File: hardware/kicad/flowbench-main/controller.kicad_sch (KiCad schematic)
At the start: 11 parts, among them J4 ESP32-S3-DevKitC-1 J1, J5 ESP32-S3-DevKitC-1 J3

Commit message: KiCad: fix off-grid pins on ADS1219 and AM26C31 symbols
A floating-point modulo misread the symbol half-height as off-grid and
shifted it by half a step, leaving top and bottom pins 0.635 mm off the
1.27 mm connection grid (16 ERC warnings). verify.py now checks every pin
and wire end against the grid.

Co-Authored-By: Claude Opus 5.5 <noreply@anthropic.com>
Claude-Session: https://claude.ai/code/session_01QEmmugJA9S77dSDSNcKrPa
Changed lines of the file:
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@@
 (text "The DevKit plugs into two 22-pin sockets. Its own 3V3 pins are left open: the board makes +3V3 separately." (at 20.32 20.32 0) (effects (font (size 1.524 1.524)) (justify left bottom)))
 (text "GPIO35-37 are used by the octal flash and PSRAM. GPIO47/48 are 1.8 V on the WROOM-2 and stay unused." (at 20.32 24.13 0) (effects (font (size 1.524 1.524)) (justify left bottom)))
-(symbol (lib_id "FlowBench:DevKitC-1_J1") (at 29.21 71.12 0) (unit 1)
-  (in_bom yes) (on_board yes) (dnp no)
-  (property "Reference" "J4" (at 20.32 38.735 0) (effects (font (size 1.27 1.27)) (justify left)))
-  (property "Value" "ESP32-S3-DevKitC-1 J1" (at 25.06 38.735 0) (effects (font (size 1.27 1.27)) (justify left)))
-  (property "Footprint" "Connector_PinSocket_2.54mm:PinSocket_1x22_P2.54mm_Vertical" (at 29.21 71.12 0) (effects (font (size 1.27 1.27)) (justify left) hide))
-  (property "Datasheet" "~" (at 29.21 71.12 0) (effects (font (size 1.27 1.27)) (justify left) hide))
+(symbol (lib_id "FlowBench:DevKitC-1_J1") (at 29.21 69.85 0) (unit 1)
+  (in_bom yes) (on_board yes) (dnp no)
+  (property "Reference" "J4" (at 20.32 38.1 0) (effects (font (size 1.27 1.27)) (justify left)))
+  (property "Value" "ESP32-S3-DevKitC-1 J1" (at 25.06 38.1 0) (effects (font (size 1.27 1.27)) (justify left)))
+  (property "Footprint" "Connector_PinSocket_2.54mm:PinSocket_1x22_P2.54mm_Vertical" (at 29.21 69.85 0) (effects (font (size 1.27 1.27)) (justify left) hide))
+  (property "Datasheet" "~" (at 29.21 69.85 0) (effects (font (size 1.27 1.27)) (justify left) hide))
   (pin "1")
   (pin "2")
@@
   (pin "21")
   (pin "22")
-  (instances (project "flowbench-main" (path "/132431a4-6ccd-4deb-a1e9-9797cfc2cdf2/a3e77ddf-1815-4e9d-bd7e-a2f9fc3f67e3" (reference "J4") (unit 1))))
+  (instances (project "flowbench-main" (path "/c152861c-b5ff-4f41-8930-02e957d22356/ba051b45-4e57-4bb8-a5b4-557957ea72a9" (reference "J4") (unit 1))))
 )
 (no_connect (at 40.64 43.18))
@@
 (wire (pts (xy 40.64 96.52) (xy 43.18 96.52)) (stroke (width 0) (type default)))
 (global_label "GND" (shape passive) (at 43.18 96.52 0) (fields_autoplaced) (effects (font (size 1.27 1.27)) (justify left)) (property "Intersheetrefs" "${INTERSHEET_REFS}" (at 43.18 96.52 0) (effects (font (size 1.27 1.27)) (justify left) hide)))
-(symbol (lib_id "FlowBench:DevKitC-1_J3") (at 97.79 71.12 0) (unit 1)
-  (in_bom yes) (on_board yes) (dnp no)
-  (property "Reference" "J5" (at 67.78 38.735 0) (effects (font (size 1.27 1.27)) (justify left)))
-  (property "Value" "ESP32-S3-DevKitC-1 J3" (at 72.52 38.735 0) (effects (font (size 1.27 1.27)) (justify left)))
-  (property "Footprint" "Connector_PinSocket_2.54mm:PinSocket_1x22_P2.54mm_Vertical" (at 97.79 71.12 0) (effects (font (size 1.27 1.27)) (justify left) hide))
-  (property "Datasheet" "~" (at 97.79 71.12 0) (effects (font (size 1.27 1.27)) (justify left) hide))
+(symbol (lib_id "FlowBench:DevKitC-1_J3") (at 97.79 69.85 0) (unit 1)
+  (in_bom yes) (on_board yes) (dnp no)
+  (property "Reference" "J5" (at 67.78 38.1 0) (effects (font (size 1.27 1.27)) (justify left)))
+  (property "Value" "ESP32-S3-DevKitC-1 J3" (at 72.52 38.1 0) (effects (font (size 1.27 1.27)) (justify left)))
+  (property "Footprint" "Connector_PinSocket_2.54mm:PinSocket_1x22_P2.54mm_Vertical" (at 97.79 69.85 0) (effects (font (size 1.27 1.27)) (justify left) hide))
+  (property "Datasheet" "~" (at 97.79 69.85 0) (effects (font (size 1.27 1.27)) (justify left) hide))
   (pin "1")
   (pin "2")
@@
   (pin "21")
   (pin "22")
-  (instances (project "flowbench-main" (path "/132431a4-6ccd-4deb-a1e9-9797cfc2cdf2/a3e77ddf-1815-4e9d-bd7e-a2f9fc3f67e3" (reference "J5") (unit 1))))
+  (instances (project "flowbench-main" (path "/c152861c-b5ff-4f41-8930-02e957d22356/ba051b45-4e57-4bb8-a5b4-557957ea72a9" (reference "J5") (unit 1))))
 )
 (wire (pts (xy 83.82 43.18) (xy 81.28 43.18)) (stroke (width 0) (type default)))
@@
   (pin "1")
   (pin "2")
-  (instances (project "flowbench-main" (path "/132431a4-6ccd-4deb-a1e9-9797cfc2cdf2/a3e77ddf-1815-4e9d-bd7e-a2f9fc3f67e3" (reference "R13") (unit 1))))
+  (instances (project "flowbench-main" (path "/c152861c-b5ff-4f41-8930-02e957d22356/ba051b45-4e57-4bb8-a5b4-557957ea72a9" (reference "R13") (unit 1))))
 )
 (wire (pts (xy 120.65 55.88) (xy 120.65 53.34)) (stroke (width 0) (type default)))
@@
   (pin "1")
   (pin "2")
-  (instances (project "flowbench-main" (path "/132431a4-6ccd-4deb-a1e9-9797cfc2cdf2/a3e77ddf-1815-4e9d-bd7e-a2f9fc3f67e3" (reference "R14") (unit 1))))
+  (instances (project "flowbench-main" (path "/c152861c-b5ff-4f41-8930-02e957d22356/ba051b45-4e57-4bb8-a5b4-557957ea72a9" (reference "R14") (unit 1))))
 )
 (wire (pts (xy 132.08 57.15) (xy 132.08 54.61)) (stroke (width 0) (type default)))
@@
   (pin "1")
   (pin "2")
-  (instances (project "flowbench-main" (path "/132431a4-6ccd-4deb-a1e9-9797cfc2cdf2/a3e77ddf-1815-4e9d-bd7e-a2f9fc3f67e3" (reference "R15") (unit 1))))
+  (instances (project "flowbench-main" (path "/c152861c-b5ff-4f41-8930-02e957d22356/ba051b45-4e57-4bb8-a5b4-557957ea72a9" (reference "R15") (unit 1))))
 )
 (wire (pts (xy 144.78 55.88) (xy 144.78 53.34)) (stroke (width 0) (type default)))
@@
   (property "Datasheet" "~" (at 156.21 44.45 0) (effects (font (size 1.27 1.27)) (justify left) hide))
   (pin "1")
-  (instances (project "flowbench-main" (path "/132431a4-6ccd-4deb-a1e9-9797cfc2cdf2/a3e77ddf-1815-4e9d-bd7e-a2f9fc3f67e3" (reference "TP7") (unit 1))))
+  (instances (project "flowbench-main" (path "/c152861c-b5ff-4f41-8930-02e957d22356/ba051b45-4e57-4bb8-a5b4-557957ea72a9" (reference "TP7") (unit 1))))
 )
 (wire (pts (xy 156.21 44.45) (xy 156.21 46.99)) (stroke (width 0) (type default)))
@@
   (property "Datasheet" "~" (at 168.91 44.45 0) (effects (font (size 1.27 1.27)) (justify left) hide))
   (pin "1")
-  (instances (project "flowbench-main" (path "/132431a4-6ccd-4deb-a1e9-9797cfc2cdf2/a3e77ddf-1815-4e9d-bd7e-a2f9fc3f67e3" (reference "TP8") (unit 1))))
+  (instances (project "flowbench-main" (path "/c152861c-b5ff-4f41-8930-02e957d22356/ba051b45-4e57-4bb8-a5b4-557957ea72a9" (reference "TP8") (unit 1))))
 )
 (wire (pts (xy 168.91 44.45) (xy 168.91 46.99)) (stroke (width 0) (type default)))
@@
   (property "Datasheet" "~" (at 180.34 44.45 0) (effects (font (size 1.27 1.27)) (justify left) hide))
   (pin "1")
-  (instances (project "flowbench-main" (path "/132431a4-6ccd-4deb-a1e9-9797cfc2cdf2/a3e77ddf-1815-4e9d-bd7e-a2f9fc3f67e3" (reference "TP9") (unit 1))))
+  (instances (project "flowbench-main" (path "/c152861c-b5ff-4f41-8930-02e957d22356/ba051b45-4e57-4bb8-a5b4-557957ea72a9" (reference "TP9") (unit 1))))
 )
 (wire (pts (xy 180.34 44.45) (xy 180.34 46.99)) (stroke (width 0) (type default)))
@@
   (property "Datasheet" "~" (at 191.77 44.45 0) (effects (font (size 1.27 1.27)) (justify left) hide))
   (pin "1")
-  (instances (project "flowbench-main" (path "/132431a4-6ccd-4deb-a1e9-9797cfc2cdf2/a3e77ddf-1815-4e9d-bd7e-a2f9fc3f67e3" (reference "TP10") (unit 1))))
+  (instances (project "flowbench-main" (path "/c152861c-b5ff-4f41-8930-02e957d22356/ba051b45-4e57-4bb8-a5b4-557957ea72a9" (reference "TP10") (unit 1))))
 )
 (wire (pts (xy 191.77 44.45) (xy 191.77 46.99)) (stroke (width 0) (type default)))
@@
   (property "Datasheet" "~" (at 203.2 44.45 0) (effects (font (size 1.27 1.27)) (justify left) hide))
   (pin "1")
-  (instances (project "flowbench-main" (path "/132431a4-6ccd-4deb-a1e9-9797cfc2cdf2/a3e77ddf-1815-4e9d-bd7e-a2f9fc3f67e3" (reference "TP11") (unit 1))))
+  (instances (project "flowbench-main" (path "/c152861c-b5ff-4f41-8930-02e957d22356/ba051b45-4e57-4bb8-a5b4-557957ea72a9" (reference "TP11") (unit 1))))
 )
 (wire (pts (xy 203.2 44.45) (xy 203.2 46.99)) (stroke (width 0) (type default)))
@@
   (property "Datasheet" "~" (at 214.63 44.45 0) (effects (font (size 1.27 1.27)) (justify left) hide))
   (pin "1")
-  (instances (project "flowbench-main" (path "/132431a4-6ccd-4deb-a1e9-9797cfc2cdf2/a3e77ddf-1815-4e9d-bd7e-a2f9fc3f67e3" (reference "TP12") (unit 1))))
+  (instances (project "flowbench-main" (path "/c152861c-b5ff-4f41-8930-02e957d22356/ba051b45-4e57-4bb8-a5b4-557957ea72a9" (reference "TP12") (unit 1))))
 )
 (wire (pts (xy 214.63 44.45) (xy 214.63 46.99)) (stroke (width 0) (type default)))

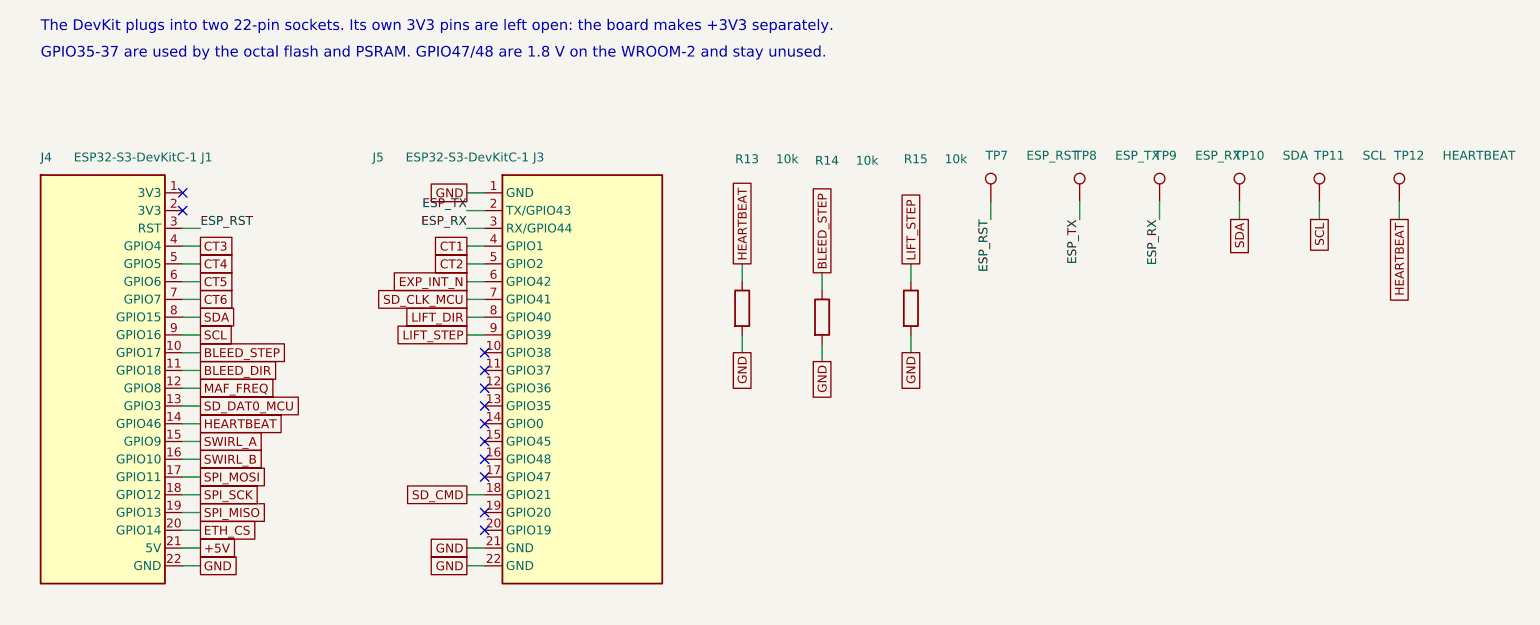
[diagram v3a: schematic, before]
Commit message: KiCad: DevKit as one part with a 25.4 mm two-row footprint
Header pinout confirmed against Espressif's J1/J3 tables; row spacing measured
at 25.4 mm. The two header symbols become one 44-pin ESP32-S3-DevKitC-1 part on
footprint FlowBench:ESP32-S3-DevKitC-1 (J1 pads 1-22, J3 pads 23-44), with the
antenna end marked. BOM notes the N32R16V as a drop-in alternative.

Co-Authored-By: Claude Opus 5.5 <noreply@anthropic.com>
Claude-Session: https://claude.ai/code/session_01QEmmugJA9S77dSDSNcKrPa
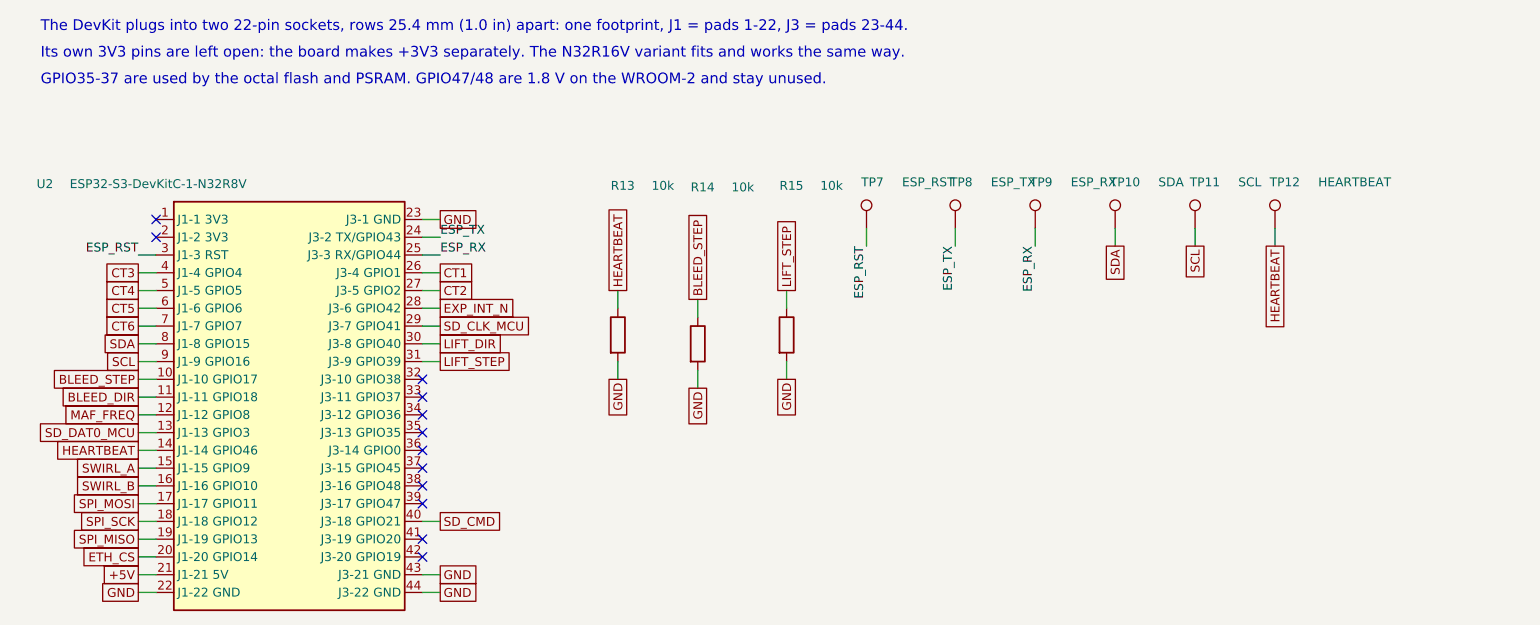
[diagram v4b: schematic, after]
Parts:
- removed J4: ESP32-S3-DevKitC-1 J1, Connector_PinSocket_2.54mm:PinSocket_1x22_P2.54mm_Vertical, symbol FlowBench:DevKitC-1_J1
- removed J5: ESP32-S3-DevKitC-1 J3, Connector_PinSocket_2.54mm:PinSocket_1x22_P2.54mm_Vertical, symbol FlowBench:DevKitC-1_J3
- added U2: ESP32-S3-DevKitC-1-N32R8V, FlowBench:ESP32-S3-DevKitC-1, symbol FlowBench:ESP32-S3-DevKitC-1
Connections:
- net +5V: now also U2.21 (J1-21 5V)
- net BLEED_DIR: now also U2.11 (J1-11 GPIO18)
- net BLEED_STEP: now also U2.10 (J1-10 GPIO17)
- net CT1: now also U2.26 (J3-4 GPIO1)
- net CT2: now also U2.27 (J3-5 GPIO2)
- net CT3: now also U2.4 (J1-4 GPIO4)
- net CT4: now also U2.5 (J1-5 GPIO5)
- net CT5: now also U2.6 (J1-6 GPIO6)
- net CT6: now also U2.7 (J1-7 GPIO7)
- net ESP_RST: now also U2.3 (J1-3 RST)
- net ESP_RX: now also U2.25 (J3-3 RX/GPIO44)
- net ESP_TX: now also U2.24 (J3-2 TX/GPIO43)
- net ETH_CS: now also U2.20 (J1-20 GPIO14)
- net EXP_INT_N: now also U2.28 (J3-6 GPIO42)
- net GND: now also U2.22 (J1-22 GND), U2.23 (J3-1 GND), U2.43 (J3-21 GND), U2.44 (J3-22 GND)
- net HEARTBEAT: now also U2.14 (J1-14 GPIO46)
- net LIFT_DIR: now also U2.30 (J3-8 GPIO40)
- net LIFT_STEP: now also U2.31 (J3-9 GPIO39)
- net MAF_FREQ: now also U2.12 (J1-12 GPIO8)
- net SCL: now also U2.9 (J1-9 GPIO16)
- net SDA: now also U2.8 (J1-8 GPIO15)
- net SD_CLK_MCU: now also U2.29 (J3-7 GPIO41)
- net SD_CMD: now also U2.40 (J3-18 GPIO21)
- net SD_DAT0_MCU: now also U2.13 (J1-13 GPIO3)
- net SPI_MISO: now also U2.19 (J1-19 GPIO13)
- net SPI_MOSI: now also U2.17 (J1-17 GPIO11)
- net SPI_SCK: now also U2.18 (J1-18 GPIO12)
- net SWIRL_A: now also U2.15 (J1-15 GPIO9)
- net SWIRL_B: now also U2.16 (J1-16 GPIO10)
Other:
- note added: "Its own 3V3 pins are left open: the board makes +3V3 separately. The N32R16V variant fits and works the same way."
- note added: "The DevKit plugs into two 22-pin sockets, rows 25.4 mm (1.0 in) apart: one footprint, J1 = pads 1-22, J3 = pads 23-44."
- note removed: "The DevKit plugs into two 22-pin sockets. Its own 3V3 pins are left open: the board makes +3V3 separately."
